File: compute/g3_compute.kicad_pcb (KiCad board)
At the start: 4 copper layers, 100 x 100 mm, 49 parts, among them J101 CONSMA001-SMD-G, J102 Temp_Connector_1x4, U101 PA1616D, U102 LoRa-E5, U201 SX1262, U202 PE4259, Y201 DNL

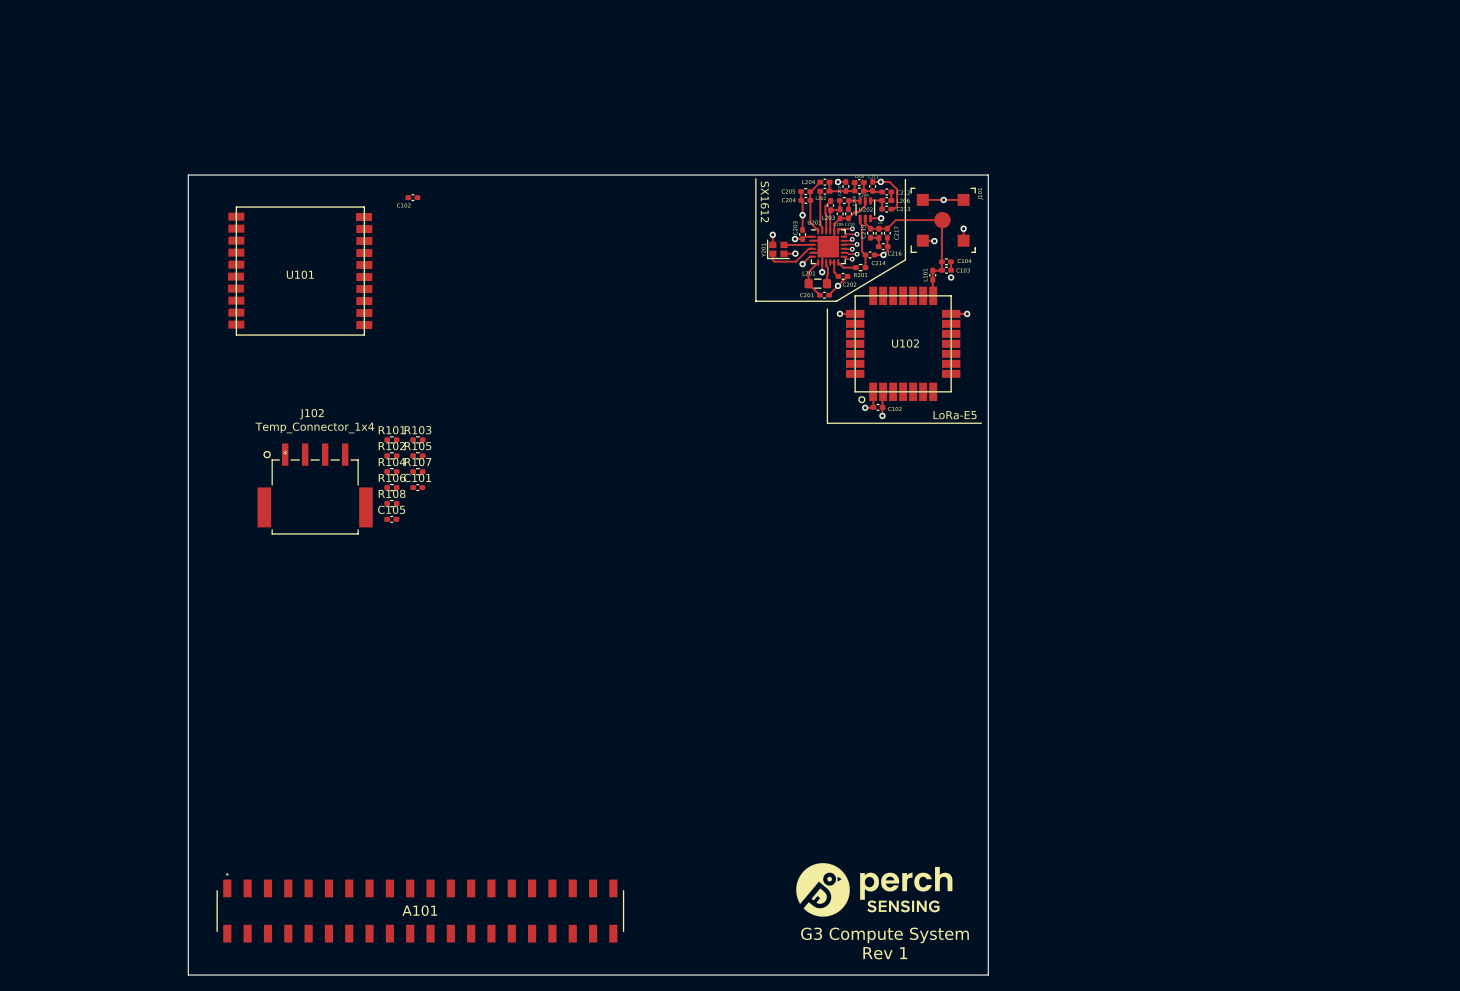
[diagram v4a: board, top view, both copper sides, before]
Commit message: test points, footprints fixes, and layout fixes
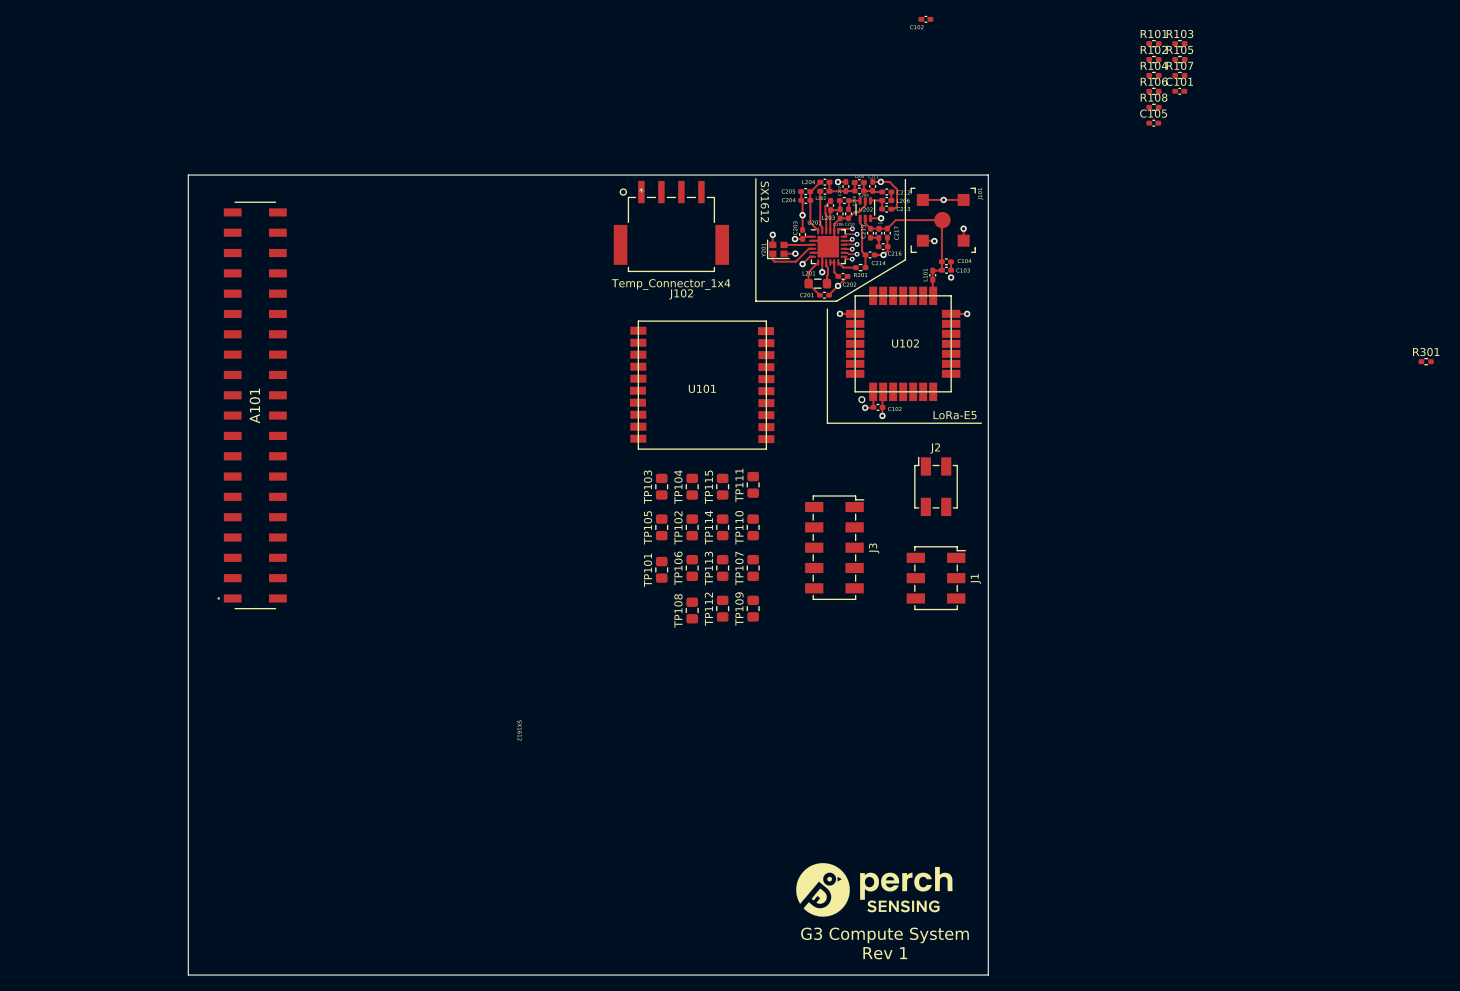
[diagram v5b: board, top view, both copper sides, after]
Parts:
- added J1: CPPC_Conn, Connector_Samtec_HLE_SMD:Samtec_HLE-103-02-xxx-DV_2x03_P2.54mm_Horizontal, F.Cu at (193.5, 90.4)
- added J2: Power_Subsystem_Conn, Connector_Samtec_HLE_SMD:Samtec_HLE-102-02-xxx-DV_2x02_P2.54mm_Horizontal, F.Cu at (193.5, 79.0)
- added J3: GPIO_Breakout_Conn, Connector_Samtec_HLE_SMD:Samtec_HLE-105-02-xxx-DV_2x05_P2.54mm_Horizontal, F.Cu at (180.8, 86.6)
- added R301: TBD, Resistor_SMD:R_0402_1005Metric_Pad0.72x0.64mm_HandSolder, F.Cu at (254.7, 63.3)
- added TP101: TestPoint, Capacitor_SMD:C_0805_2012Metric_Pad1.18x1.45mm_HandSolder, F.Cu at (159.2, 89.4)
- added TP102: TestPoint, Capacitor_SMD:C_0805_2012Metric_Pad1.18x1.45mm_HandSolder, F.Cu at (163.0, 84.0)
- added TP103: TestPoint, Capacitor_SMD:C_0805_2012Metric_Pad1.18x1.45mm_HandSolder, F.Cu at (159.2, 79.0)
- added TP104: TestPoint, Capacitor_SMD:C_0805_2012Metric_Pad1.18x1.45mm_HandSolder, F.Cu at (163.0, 79.0)
- added TP105: TestPoint, Capacitor_SMD:C_0805_2012Metric_Pad1.18x1.45mm_HandSolder, F.Cu at (159.2, 84.0)
- added TP106: TestPoint, Capacitor_SMD:C_0805_2012Metric_Pad1.18x1.45mm_HandSolder, F.Cu at (163.0, 89.1)
- added TP107: TestPoint, Capacitor_SMD:C_0805_2012Metric_Pad1.18x1.45mm_HandSolder, F.Cu at (170.6, 89.1)
- added TP108: TestPoint, Capacitor_SMD:C_0805_2012Metric_Pad1.18x1.45mm_HandSolder, F.Cu at (163.0, 94.4)
- added TP109: TestPoint, Capacitor_SMD:C_0805_2012Metric_Pad1.18x1.45mm_HandSolder, F.Cu at (170.6, 94.2)
- added TP110: TestPoint, Capacitor_SMD:C_0805_2012Metric_Pad1.18x1.45mm_HandSolder, F.Cu at (170.6, 84.0)
- added TP111: TestPoint, Capacitor_SMD:C_0805_2012Metric_Pad1.18x1.45mm_HandSolder, F.Cu at (170.6, 78.7)
- added TP112: TestPoint, Capacitor_SMD:C_0805_2012Metric_Pad1.18x1.45mm_HandSolder, F.Cu at (166.8, 94.2)
- added TP113: TestPoint, Capacitor_SMD:C_0805_2012Metric_Pad1.18x1.45mm_HandSolder, F.Cu at (166.8, 89.1)
- added TP114: TestPoint, Capacitor_SMD:C_0805_2012Metric_Pad1.18x1.45mm_HandSolder, F.Cu at (166.8, 84.0)
- added TP115: TestPoint, Capacitor_SMD:C_0805_2012Metric_Pad1.18x1.45mm_HandSolder, F.Cu at (166.8, 79.0)
- Y201: value DNL -> TBD
- moved C105 107.4 mm to (220.7, 33.5)
- moved C101 107.4 mm to (223.9, 29.5)
- moved R103 107.4 mm to (223.9, 23.6)
- moved R105 107.4 mm to (223.9, 25.6)
- moved R107 107.4 mm to (223.9, 27.6)
- moved R101 107.4 mm to (220.7, 23.6)
- moved R102 107.4 mm to (220.7, 25.6)
- moved R104 107.4 mm to (220.7, 27.6)
- moved R106 107.4 mm to (220.7, 29.5)
- moved R108 107.4 mm to (220.7, 31.5)
- moved C102 67.9 mm to (192.2, 20.5)
- moved A101 66.5 mm to (108.4, 68.8), turned to 270 degrees
- moved J102 55.3 mm to (156.6, 42.1)
- moved U101 52.2 mm to (164.2, 66.3)
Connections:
- net Net-(A101-Pad5) renamed /PI_SCL
- A101 pad 1: Net-(A101-Pad1) -> 3V3
- A101 pad 10: Net-(A101-Pad10) -> /PI_RX0
- A101 pad 11: Net-(A101-Pad11) -> /PI_GPIO17
- A101 pad 12: Net-(A101-Pad12) -> /PI_GPIO18
- A101 pad 13: Net-(A101-Pad13) -> /PI_GPIO27
- A101 pad 14: Net-(A101-Pad14) -> GND
- A101 pad 15: Net-(A101-Pad15) -> /PI_GPIO22
- A101 pad 16: Net-(A101-Pad16) -> /PI_GPIO23
- A101 pad 17: Net-(A101-Pad17) -> 3V3
- A101 pad 18: Net-(A101-Pad18) -> /PI_GPIO24
- A101 pad 19: Net-(A101-Pad19) -> /PI_SDI
- A101 pad 2: Net-(A101-Pad2) -> 5V
- A101 pad 20: Net-(A101-Pad20) -> GND
- A101 pad 21: Net-(A101-Pad21) -> /PI_SDO
- A101 pad 22: Net-(A101-Pad22) -> /PI_GPIO25
- A101 pad 23: Net-(A101-Pad23) -> /PI_SCLK
- A101 pad 24: Net-(A101-Pad24) -> /~PI_CE0
- A101 pad 25: Net-(A101-Pad25) -> GND
- A101 pad 26: Net-(A101-Pad26) -> /PI_GPIO7
- A101 pad 29: Net-(A101-Pad29) -> /~GPS_RESET
- A101 pad 3: Net-(A101-Pad3) -> /PI_SDA
- A101 pad 30: Net-(A101-Pad30) -> GND
- A101 pad 31: Net-(A101-Pad31) -> /GPS_SW_EN
- A101 pad 32: Net-(A101-Pad32) -> /PI_INT
- A101 pad 33: Net-(A101-Pad33) -> /~SX_RESET
- A101 pad 34: Net-(A101-Pad34) -> GND
- A101 pad 35: Net-(A101-Pad35) -> /PI_TX1
- A101 pad 36: Net-(A101-Pad36) -> /~E5_RESET
- A101 pad 37: Net-(A101-Pad37) -> /PI_RX1
- A101 pad 38: Net-(A101-Pad38) -> /PI_TX2
- A101 pad 39: Net-(A101-Pad39) -> GND
- A101 pad 4: Net-(A101-Pad4) -> 5V
- A101 pad 40: Net-(A101-Pad40) -> /PI_RX2
- A101 pad 6: Net-(A101-Pad6) -> GND
- A101 pad 7: Net-(A101-Pad7) -> /PI_GPIO4
- A101 pad 8: Net-(A101-Pad8) -> /PI_TX0
- A101 pad 9: Net-(A101-Pad9) -> GND
- J102 pad 4: /Temp_SCL -> /PI_SDL
- R104 pad 1: /PI_SDI -> /PI_SDL
- R105 pad 1: /PPT_RX0 -> /CPPC_RX0
- R106 pad 1: /PPT_TX0 -> /CPPC_TX0

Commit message: Adjusting board connectors
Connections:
- A101 pad 4: 5V -> Net-(A101-Pad4)
- R201 pad 2: /LoRa Module/DIO2 -> /SX1262 LoRa Module/DIO2

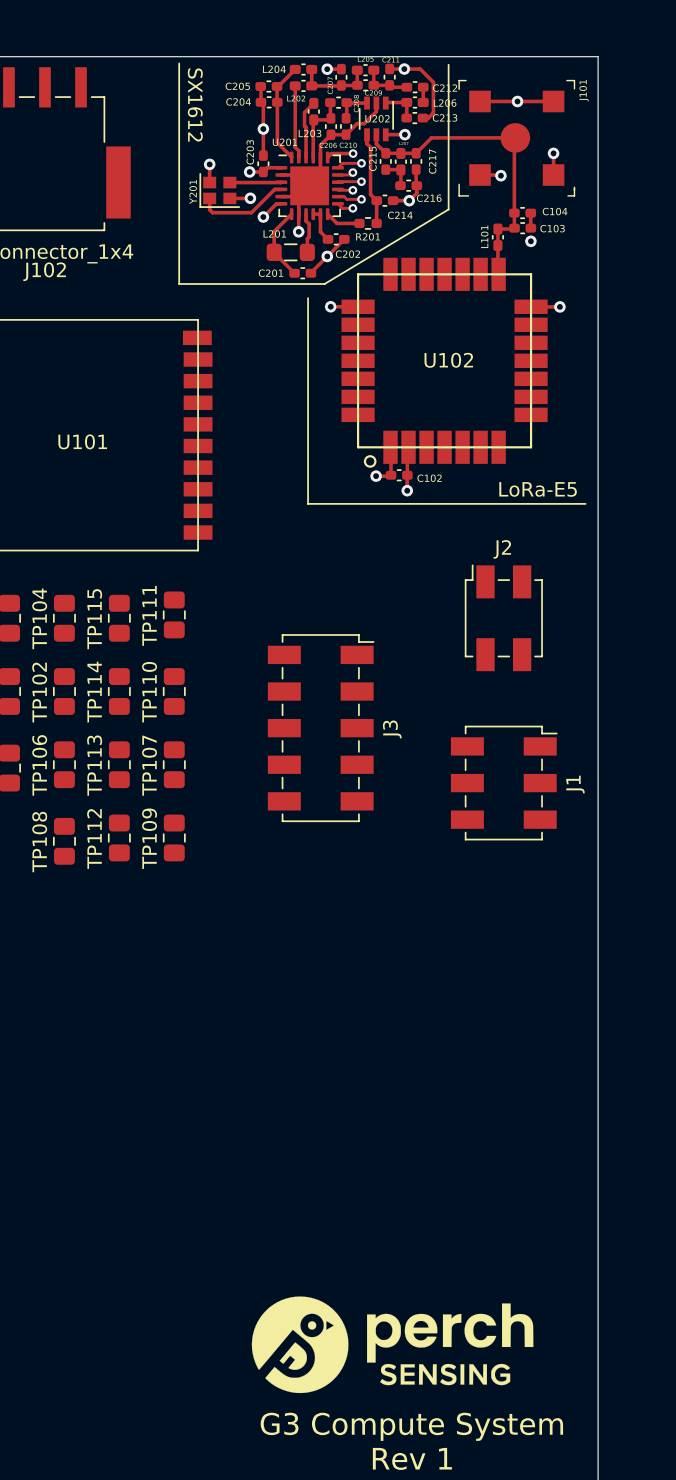
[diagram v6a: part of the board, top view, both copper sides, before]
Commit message: Adjusting connectors foot prints
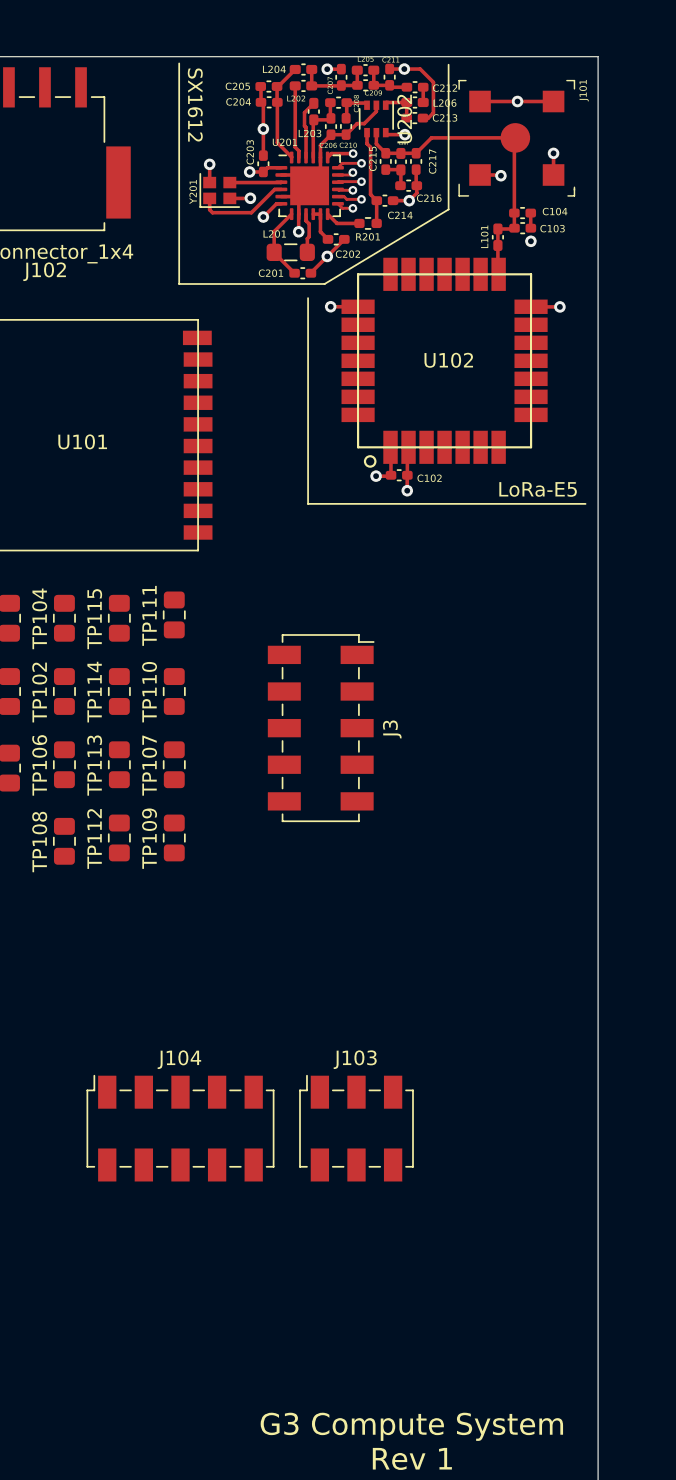
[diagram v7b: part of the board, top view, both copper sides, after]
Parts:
- removed G***: LOGO, Perch:perch_logo
- removed J1: CPPC_Conn, Connector_Samtec_HLE_SMD:Samtec_HLE-103-02-xxx-DV_2x03_P2.54mm_Horizontal
- removed J2: Power_Subsystem_Conn, Connector_Samtec_HLE_SMD:Samtec_HLE-102-02-xxx-DV_2x02_P2.54mm_Horizontal
- added J103: Conn_02x03_Counter_Clockwise, Connector_Samtec_HLE_SMD:Samtec_HLE-103-02-xxx-DV_2x03_P2.54mm_Horizontal, F.Cu at (183.2, 114.4)
- added J104: Conn_Power_Compute_02x05, Connector_Samtec_HLE_SMD:Samtec_HLE-105-02-xxx-DV_2x05_P2.54mm_Horizontal, F.Cu at (171.0, 114.4)
- U202: footprint Package_TO_SOT_SMD:Texas_R-PDSO-G6 -> Package_TO_SOT_SMD:SOT-363_SC-70-6
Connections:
- net /LoRa Module/BUSY renamed /SX1262 LoRa Module/BUSY
- net /LoRa Module/DIO1 renamed /SX1262 LoRa Module/DIO1
- net /LoRa Module/DIO3 renamed /SX1262 LoRa Module/DIO3
- U201 pad 12: /LoRa Module/DIO2 -> /SX1262 LoRa Module/DIO2
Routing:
- net /SX1262 LoRa Module/DIO2: track 0.00 -> 2.47 mm
- net /LoRa Module/DIO2: track 2.47 -> 0.00 mm

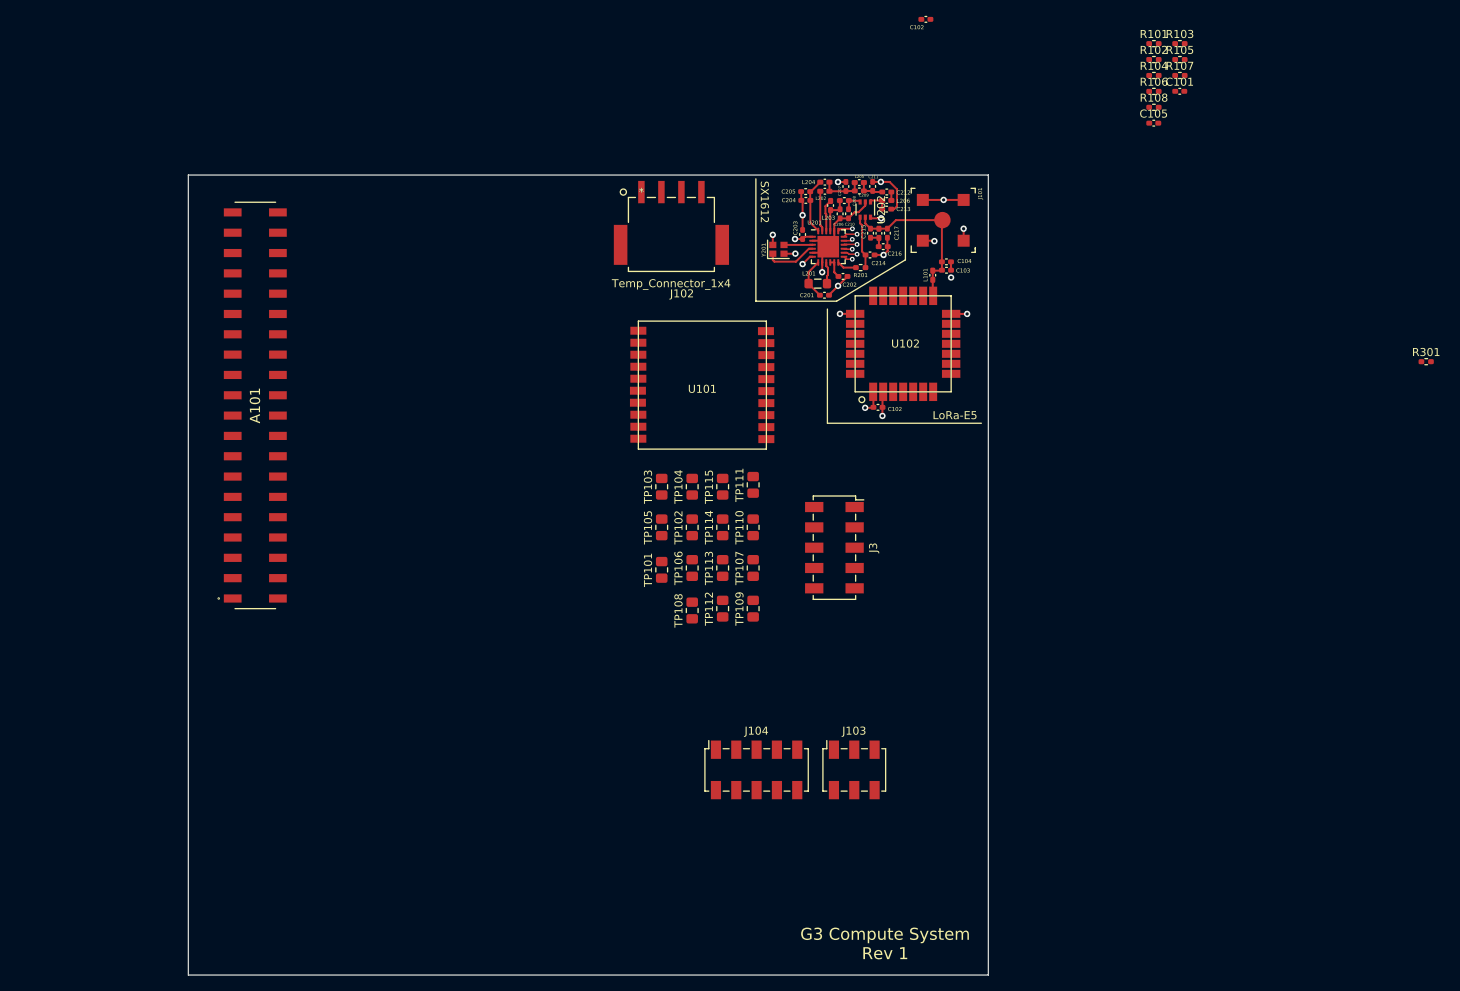
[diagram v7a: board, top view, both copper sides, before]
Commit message: First preliminary layout of pcb
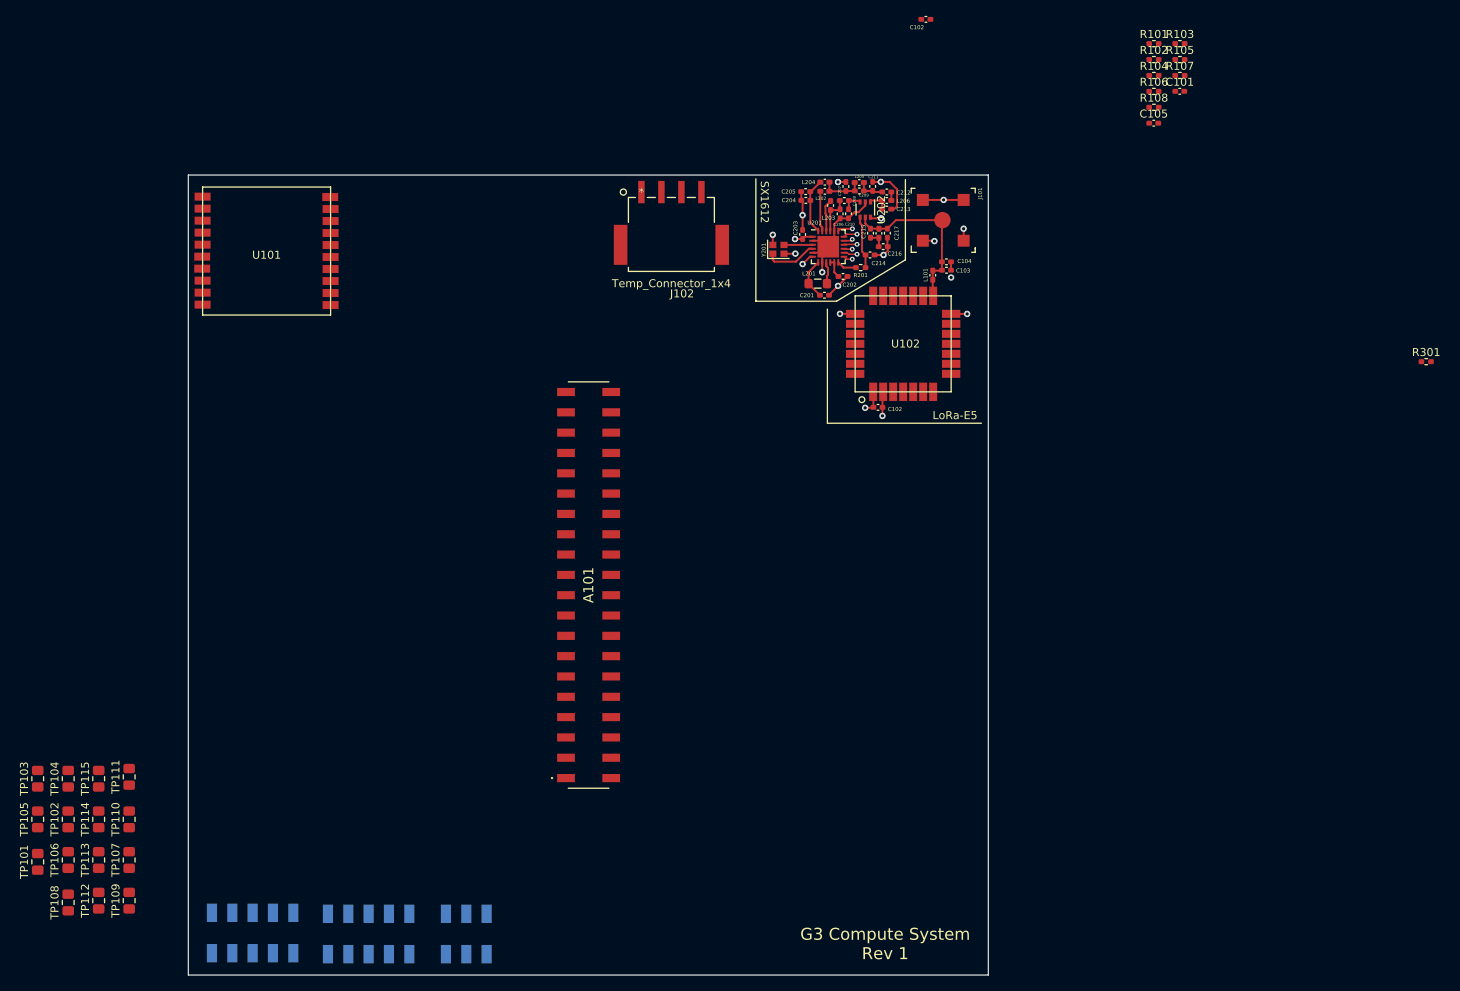
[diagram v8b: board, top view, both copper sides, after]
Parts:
- J103, J104, J3: moved to B.Cu
- moved J3 87.2 mm to (108.0, 134.8), turned to 0 degrees
- moved TP107 86.1 mm to (92.6, 125.6)
- moved TP110 86.1 mm to (92.6, 120.5)
- moved TP111 86.1 mm to (92.6, 115.2)
- moved TP101 86.1 mm to (81.2, 125.9)
- moved TP102 86.1 mm to (85.0, 120.5)
- moved TP103 86.1 mm to (81.2, 115.5)
- moved TP104 86.1 mm to (85.0, 115.5)
- moved TP105 86.1 mm to (81.2, 120.5)
- moved TP106 86.1 mm to (85.0, 125.6)
- moved TP108 86.1 mm to (85.0, 130.9)
- moved TP109 86.1 mm to (92.6, 130.7)
- moved TP113 86.1 mm to (88.8, 125.6)
- moved TP114 86.1 mm to (88.8, 120.5)
- moved TP115 86.1 mm to (88.8, 115.5)
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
